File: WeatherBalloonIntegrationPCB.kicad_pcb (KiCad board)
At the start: 2 copper layers, 90 x 90 mm, 10 parts, among them U1 ESP-32S

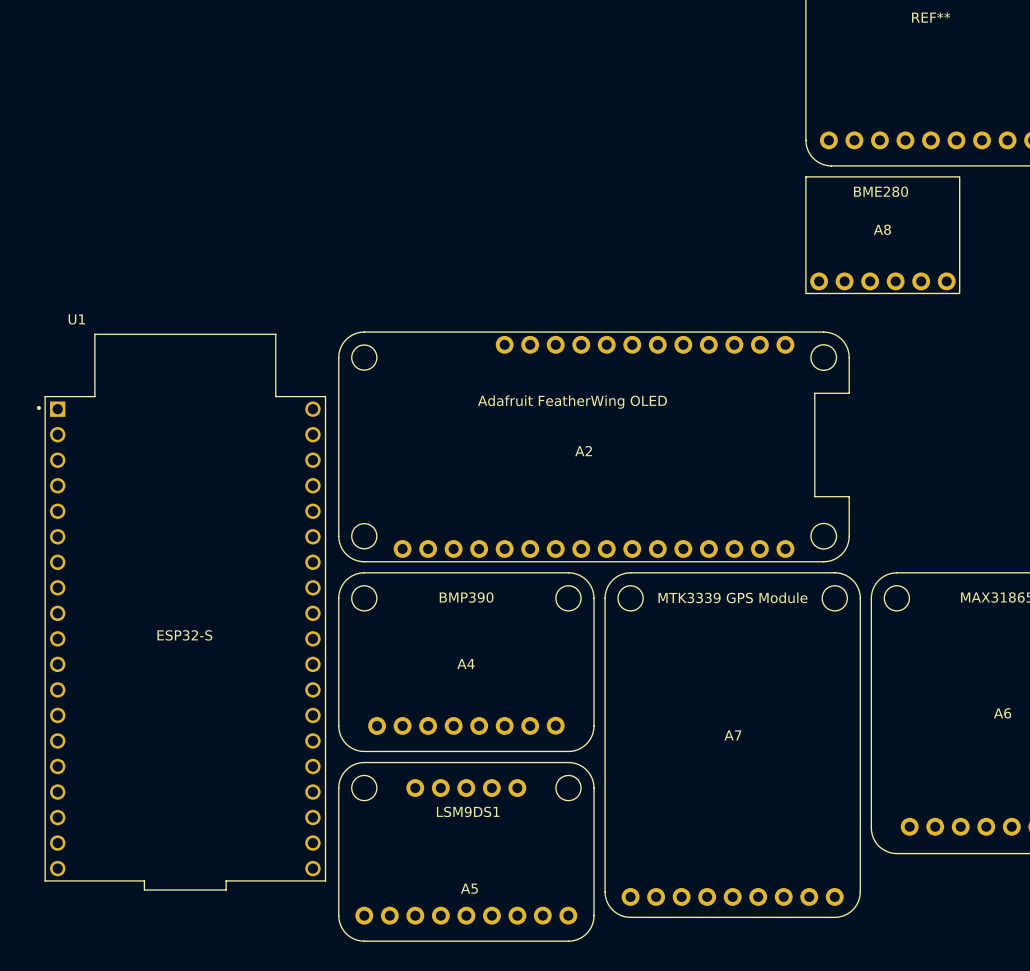
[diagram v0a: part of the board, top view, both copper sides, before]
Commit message: Connected most sensors
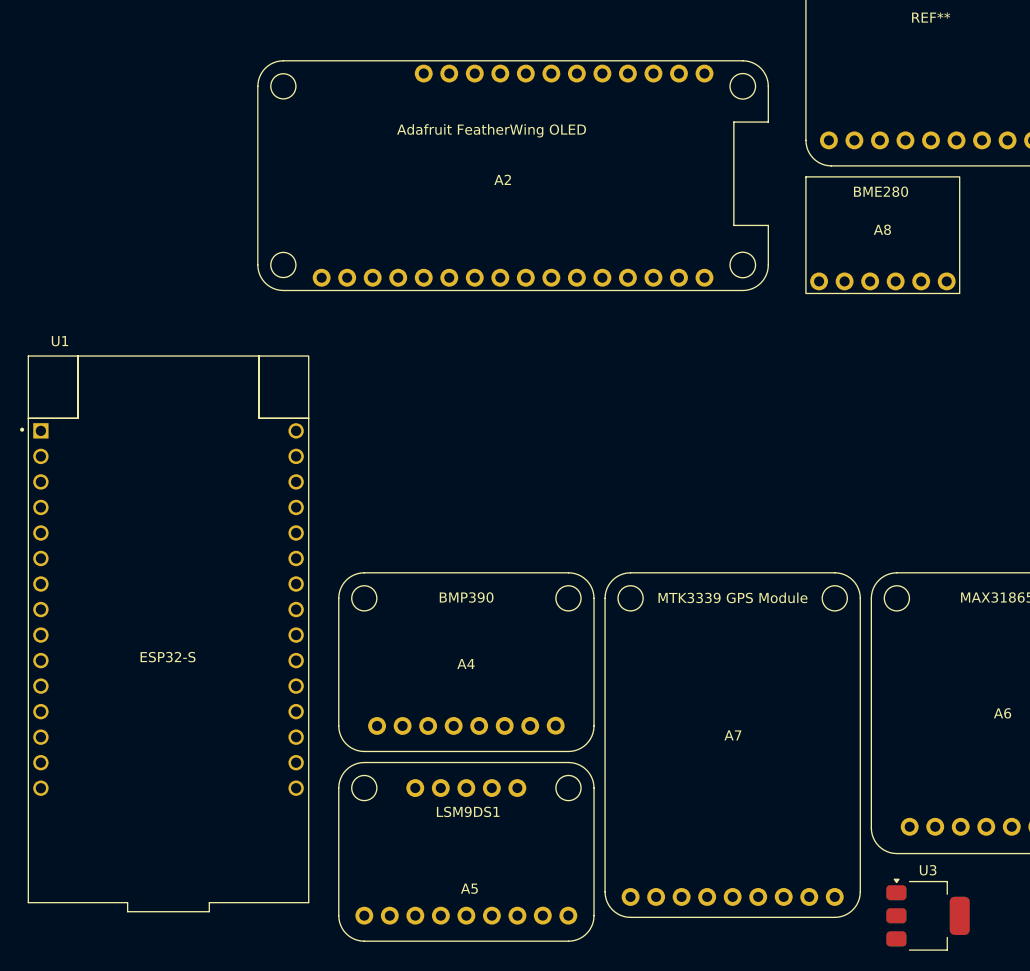
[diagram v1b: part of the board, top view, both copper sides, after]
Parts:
- added U3: AMS1117-3.3, Package_TO_SOT_SMD:SOT-223-3_TabPin2, F.Cu at (106.1, 170.2)
- moved A2 28.2 mm to (63.8, 97.5)
- moved U1 2.73 mm to (30.5, 144.8)
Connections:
- A1 pad 8: unconnected-(A1-VIN-Pad8) -> +BATT
- A3 pad 1: unconnected-(A3-VIN-Pad1) -> +3.3V
- A3 pad 5: unconnected-(A3-SCK-Pad5) -> SCK
- A3 pad 6: unconnected-(A3-MISO-Pad6) -> SDO
- A3 pad 7: unconnected-(A3-MOSI-Pad7) -> SDI
- A3 pad 8: unconnected-(A3-CS-Pad8) -> CS_MAX
- A6 pad 1: unconnected-(A6-VIN-Pad1) -> +3.3V
- A6 pad 4: unconnected-(A6-CLK-Pad4) -> SCK
- A6 pad 5: unconnected-(A6-SDO-Pad5) -> SDO
- A6 pad 6: unconnected-(A6-SDI-Pad6) -> SDI
- A6 pad 7: unconnected-(A6-CS-Pad7) -> CS_MAX
- A8 pad 1: unconnected-(A8-VCC-Pad1) -> +3.3V
- U1 pad 14: unconnected-(U1-GND1-Pad14) -> GND
- U1 pad 24: unconnected-(U1-IO2-Pad24) -> GND
- U1 pad 30: unconnected-(U1-IO18-Pad30) -> GND
- U2 pad 1: unconnected-(U2-GND-Pad1) -> GND
- U2 pad 2: unconnected-(U2-VCC-Pad2) -> +3.3V
- U2 pad 3: unconnected-(U2-MISO-Pad3) -> SDO
- U2 pad 4: unconnected-(U2-MOSI-Pad4) -> SDI
- U2 pad 5: unconnected-(U2-SCK-Pad5) -> SCK
- U2 pad 6: unconnected-(U2-CS-Pad6) -> CS_MAX
